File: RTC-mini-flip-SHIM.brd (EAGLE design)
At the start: 17.8 x 20.3 mm, 11 parts, among them IC1 DS3231/SO

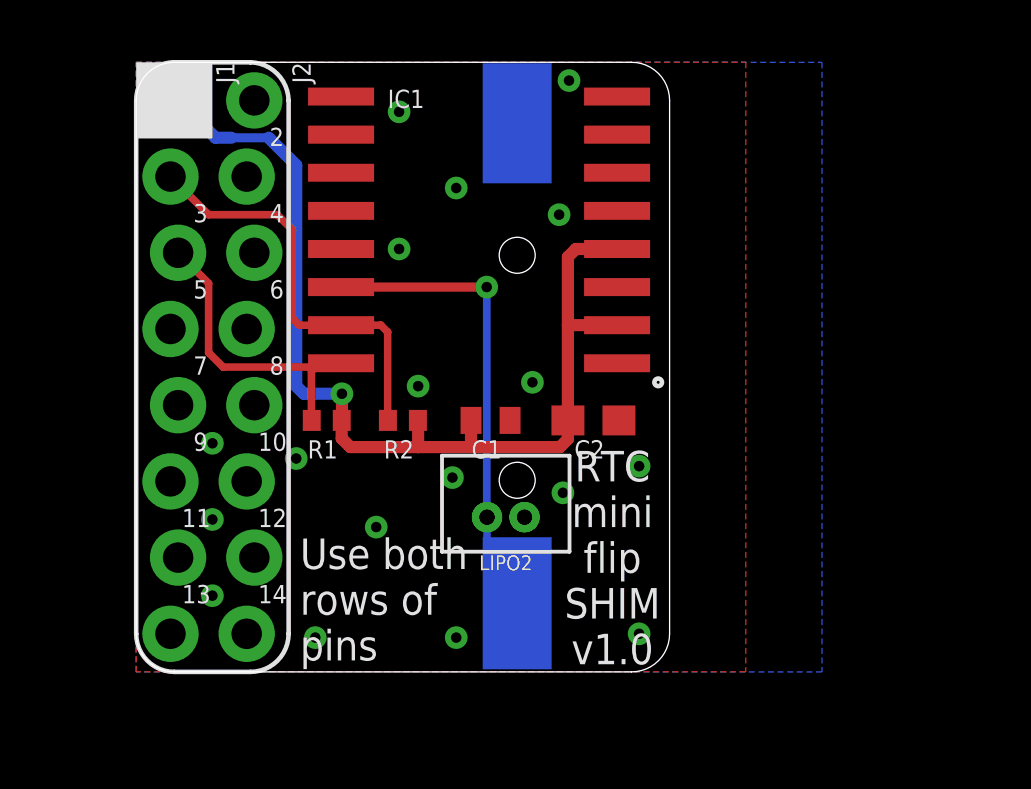
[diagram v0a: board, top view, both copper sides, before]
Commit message: Moved some stuff around. Add second footprint. Moved battery away from center for better flipability.
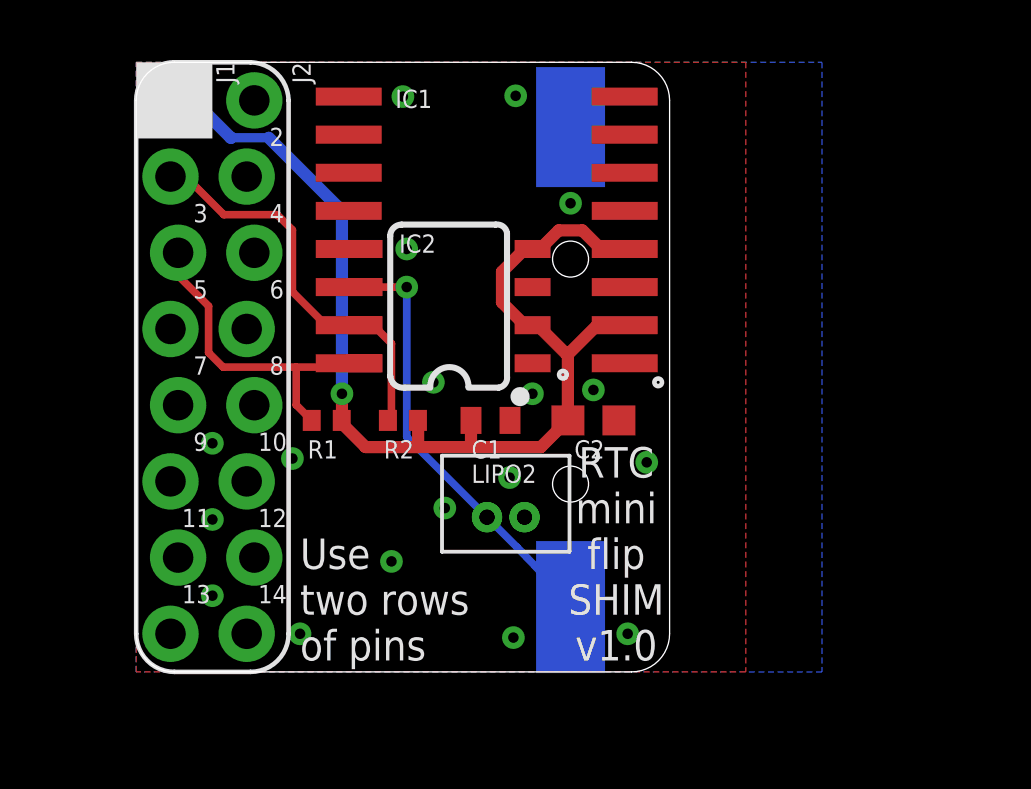
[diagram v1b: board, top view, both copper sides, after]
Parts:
- added IC2: DS3231M, SparkFun-Clocks:SO08
- moved LOGO1 1.91 mm to (23.2, 3.56)
- moved BAT1 1.78 mm to (14.5, 10.2)
- moved IC1 0.25 mm to (11.7, 14.7)
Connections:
- net 3.3V: now also IC2.2, IC2.4
- net GND: now also IC2.5
- net SCL: now also IC2.8
- net SDA: now also IC2.7
- net VBAT: now also IC2.6
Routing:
- net 3.3V: track 34.4 -> 37.5 mm
- net VBAT: track 15.8 -> 14.8 mm
- net SDA: track 14.1 -> 13.5 mm
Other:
- board text added: "Use two rows of pins"
- board text removed: "Use both rows of pins"

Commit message: Changed mini SHIM layout. Traced mini SHIM.
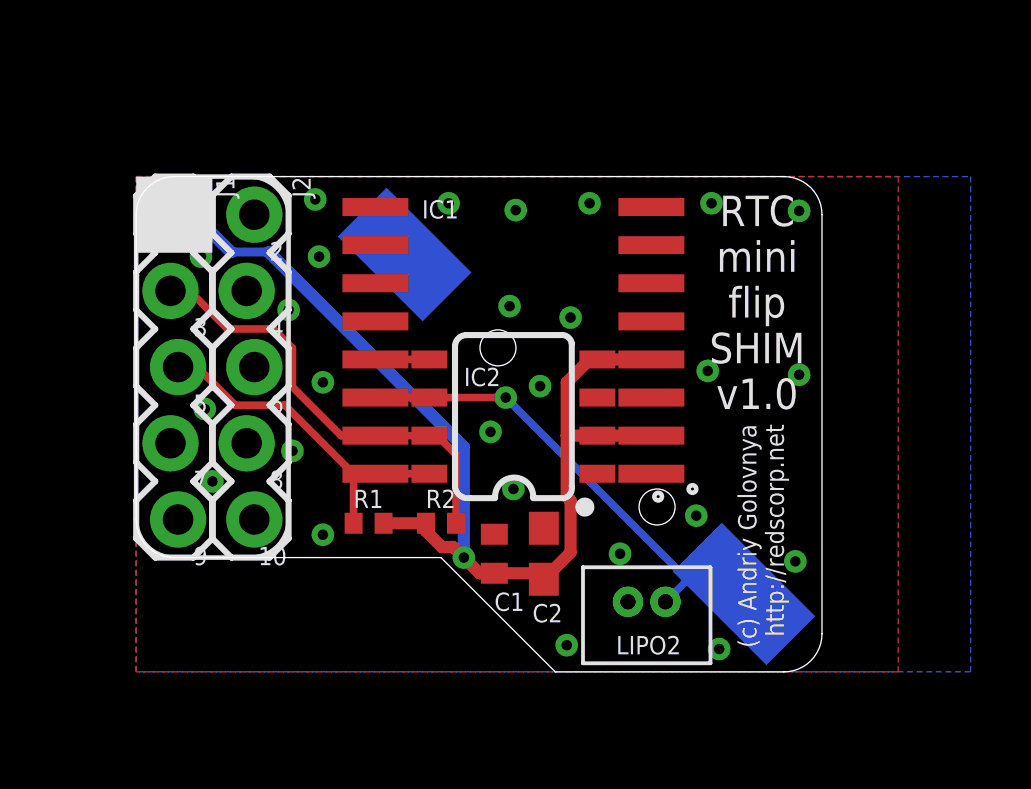
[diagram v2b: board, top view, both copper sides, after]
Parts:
- J1, J2: device SparkFun-Connectors:1X08_LOCK_NO_SILK -> SparkFun-Connectors:1X05_LOCK
- moved LIPO1 5.48 mm to (17.0, 2.34), turned to 0 degrees
- moved LIPO2 5.48 mm to (17.0, 2.34), turned to 180 degrees
- moved C2 4.74 mm to (13.6, 3.94), turned to 90 degrees
- moved C1 4.45 mm to (11.9, 3.94), turned to 90 degrees
- moved IC2 4.27 mm to (12.6, 8.51)
- moved J1 3.81 mm to (1.27, 15.2)
- moved J2 3.81 mm to (3.81, 15.2)
- moved IC1 3.79 mm to (12.6, 11.0)
- moved R1 3.70 mm to (7.75, 4.95)
- moved R2 3.66 mm to (10.2, 4.95), turned to 180 degrees
- moved BAT1 1.91 mm to (14.6, 8.26), turned to 315 degrees
- moved LOGO1 1.66 mm to (23.1, 1.91)
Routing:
- net 3.3V: track 37.5 -> 35.6 mm
- net GND: track 0.00 -> 1.80 mm, vias 18 -> 26
- net SDA: track 13.5 -> 14.8 mm
- net VBAT: track 14.8 -> 16.1 mm
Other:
- board size 17.8 x 20.3 mm -> 22.9 x 16.5 mm
- board text added: "+"
- board text added: "-"
- board text removed: "11"
- board text removed: "12"
- board text removed: "13"
- board text removed: "14"
- board text removed: "Use one rows of pins"
- board text removed: "Use two rows of pins"

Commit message: Use more locking pin headers. Moved some traces.
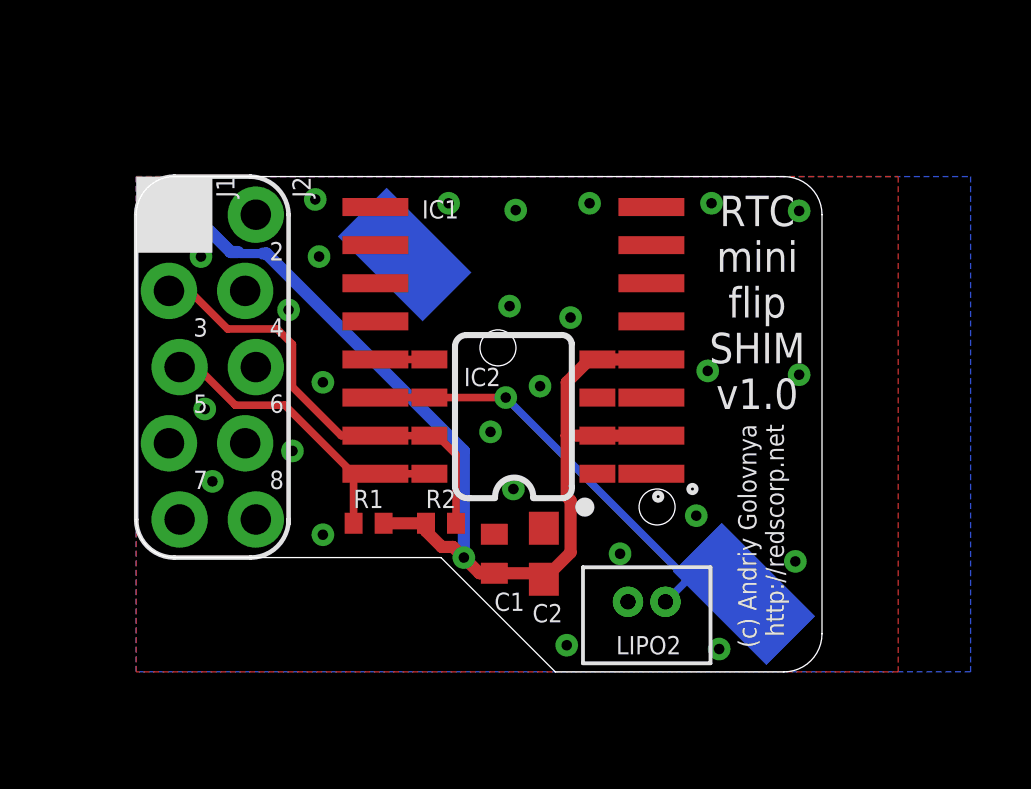
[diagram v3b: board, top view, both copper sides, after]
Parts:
- J1, J2: device SparkFun-Connectors:1X05_LOCK -> _my_locked_connectors:1X05_LOCK
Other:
- board text removed: "10"
- board text removed: "9"
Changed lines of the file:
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@@
 <layer number="115" name="ReferenceISLANDS" color="7" fill="1" visible="no" active="yes"/>
 <layer number="116" name="Patch_BOT" color="9" fill="4" visible="no" active="yes"/>
+<layer number="117" name="PM_Ref" color="7" fill="1" visible="no" active="no"/>
 <layer number="118" name="Rect_Pads" color="7" fill="1" visible="no" active="no"/>
+<layer number="119" name="PF_Ref" color="7" fill="1" visible="no" active="no"/>
+<layer number="120" name="WFL_Ref" color="7" fill="1" visible="no" active="no"/>
 <layer number="121" name="_tsilk" color="7" fill="1" visible="no" active="yes"/>
 <layer number="122" name="_bsilk" color="7" fill="1" visible="no" active="yes"/>
@@
 <layer number="128" name="_bValues" color="7" fill="1" visible="no" active="yes"/>
 <layer number="129" name="Mask" color="7" fill="1" visible="yes" active="yes"/>
+<layer number="130" name="SMDSTROOK" color="7" fill="1" visible="no" active="no"/>
 <layer number="131" name="tAdjust" color="7" fill="1" visible="no" active="yes"/>
 <layer number="132" name="bAdjust" color="7" fill="1" visible="no" active="yes"/>
+<layer number="133" name="bottom_silk" color="7" fill="1" visible="no" active="no"/>
+<layer number="134" name="silk_top" color="7" fill="1" visible="no" active="no"/>
+<layer number="135" name="silk_bottom" color="7" fill="1" visible="no" active="no"/>
+<layer number="136" name="silktop" color="7" fill="1" visible="no" active="no"/>
+<layer number="137" name="silkbottom" color="7" fill="1" visible="no" active="no"/>
+<layer number="138" name="EEE" color="7" fill="1" visible="no" active="no"/>
+<layer number="139" name="_tKeepout" color="7" fill="1" visible="no" active="no"/>
+<layer number="140" name="mbKeepout" color="7" fill="1" visible="no" active="no"/>
+<layer number="141" name="ASSEMBLY_TOP" color="7" fill="1" visible="no" active="no"/>
+<layer number="142" name="mbRestrict" color="7" fill="1" visible="no" active="no"/>
+<layer number="143" name="PLACE_BOUND_TOP" color="7" fill="1" visible="no" active="no"/>
 <layer number="144" name="Drill_legend" color="7" fill="1" visible="no" active="yes"/>
+<layer number="145" name="DrillLegend_01-16" color="7" fill="1" visible="no" active="no"/>
+<layer number="146" name="DrillLegend_01-20" color="7" fill="1" visible="no" active="no"/>
+<layer number="147" name="PIN_NUMBER" color="7" fill="1" visible="no" active="no"/>
+<layer number="148" name="DrillLegend_01-20" color="7" fill="1" visible="no" active="no"/>
+<layer number="149" name="DrillLegend_02-15" color="7" fill="1" visible="no" active="no"/>
 <layer number="150" name="Notes" color="7" fill="1" visible="no" active="yes"/>
 <layer number="151" name="HeatSink" color="7" fill="1" visible="no" active="yes"/>
@@
 <layer number="164" name="tRubout" color="7" fill="1" visible="yes" active="yes"/>
 <layer number="165" name="bRubout" color="7" fill="1" visible="yes" active="yes"/>
+<layer number="166" name="AntennaArea" color="7" fill="1" visible="no" active="no"/>
 <layer number="167" name="Fiducials" color="7" fill="1" visible="yes" active="yes"/>
+<layer number="168" name="4mmHeightArea" color="7" fill="1" visible="no" active="no"/>
 <layer number="169" name="internal" color="7" fill="1" visible="yes" active="yes"/>
+<layer number="191" name="mNets" color="7" fill="1" visible="no" active="no"/>
+<layer number="192" name="mBusses" color="7" fill="1" visible="no" active="no"/>
+<layer number="193" name="mPins" color="7" fill="1" visible="no" active="no"/>
+<layer number="194" name="mSymbols" color="7" fill="1" visible="no" active="no"/>
+<layer number="195" name="mNames" color="7" fill="1" visible="no" active="no"/>
+<layer number="196" name="mValues" color="7" fill="1" visible="no" active="no"/>
 <layer number="199" name="Contour" color="7" fill="1" visible="no" active="yes"/>
 <layer number="200" name="200bmp" color="1" fill="10" visible="no" active="yes"/>
@@
 <text x="1.905" y="6.096" size="0.6096" layer="21" font="vector" ratio="12">7</text>
 <text x="4.445" y="6.096" size="0.6096" layer="21" font="vector" ratio="12">8</text>
-<text x="1.905" y="3.556" size="0.6096" layer="21" font="vector" ratio="12">9</text>
-<text x="4.064" y="3.556" size="0.6096" layer="21" font="vector" ratio="12">10</text>
 <text x="0.635" y="11.176" size="0.6096" layer="22" font="vector" ratio="12" rot="MR0">3</text>
 <text x="0.635" y="8.636" size="0.6096" layer="22" font="vector" ratio="12" rot="MR0">5</text>
 <text x="0.635" y="6.096" size="0.6096" layer="22" font="vector" ratio="12" rot="MR0">7</text>
-<text x="0.635" y="3.556" size="0.6096" layer="22" font="vector" ratio="12" rot="MR0">9</text>
 <circle x="18.542" y="6.096" radius="0.127" width="0.1524" layer="21"/>
 <wire x1="5.08" y1="5.08" x2="3.81" y2="3.81" width="0.1524" layer="21" curve="-90"/>
@@
 <attribute name="VALUE" x="9.525" y="14.097" size="0.6096" layer="27" font="vector"/>
 </element>
-<element name="J1" library="SparkFun-Connectors" library_urn="urn:adsk.eagle:library:513" package="1X05_LOCK" package3d_urn="urn:adsk.eagle:package:38105/1" value="" x="1.27" y="15.24" smashed="yes" rot="R270">
+<element name="J1" library="_my_locked_connectors" package="1X05_LOCK" value="" x="1.27" y="15.24" smashed="yes" rot="R270">
 <attribute name="NAME" x="2.667" y="16.51" size="0.6096" layer="25" font="vector" rot="R270"/>
 <attribute name="VALUE" x="-0.762" y="16.51" size="0.6096" layer="27" font="vector" ratio="20" rot="R270"/>
 </element>
-<element name="J2" library="SparkFun-Connectors" library_urn="urn:adsk.eagle:library:513" package="1X05_LOCK" package3d_urn="urn:adsk.eagle:package:38105/1" value="" x="3.81" y="15.24" smashed="yes" rot="R270">
+<element name="J2" library="_my_locked_connectors" package="1X05_LOCK" value="" x="3.81" y="15.24" smashed="yes" rot="R270">
 <attribute name="NAME" x="5.207" y="16.51" size="0.6096" layer="25" font="vector" rot="R270"/>
 <attribute name="VALUE" x="1.778" y="16.51" size="0.6096" layer="27" font="vector" ratio="20" rot="R270"/>
@@
 <contactref element="J1" pad="3"/>
 <wire x1="3.302" y1="8.89" x2="2.032" y2="10.16" width="0.254" layer="1"/>
-<wire x1="1.397" y1="10.16" x2="2.032" y2="10.16" width="0.254" layer="1"/>
+<wire x1="1.4478" y1="10.16" x2="2.032" y2="10.16" width="0.254" layer="1"/>
 <wire x1="4.953" y1="8.89" x2="3.302" y2="8.89" width="0.254" layer="1"/>
 <wire x1="7.239" y1="6.604" x2="4.953" y2="8.89" width="0.254" layer="1"/>
@@
 <contactref element="R2" pad="1"/>
 <contactref element="J1" pad="2"/>
-<wire x1="1.143" y1="12.7" x2="1.778" y2="12.7" width="0.254" layer="1"/>
+<wire x1="1.0922" y1="12.7" x2="1.778" y2="12.7" width="0.254" layer="1"/>
 <wire x1="3.048" y1="11.43" x2="1.778" y2="12.7" width="0.254" layer="1"/>
-<wire x1="3.048" y1="11.43" x2="4.572" y2="11.43" width="0.254" layer="1"/>
-<wire x1="4.572" y1="11.43" x2="5.207" y2="10.795" width="0.254" layer="1"/>
-<wire x1="5.207" y1="9.4996" x2="5.207" y2="10.795" width="0.254" layer="1"/>
+<wire x1="3.048" y1="11.43" x2="4.699" y2="11.43" width="0.254" layer="1"/>
+<wire x1="4.699" y1="11.43" x2="5.207" y2="10.922" width="0.254" layer="1"/>
+<wire x1="5.207" y1="9.4996" x2="5.207" y2="10.922" width="0.254" layer="1"/>
 <contactref element="IC2" pad="7"/>
 <wire x1="7.973" y1="7.874" x2="6.8326" y2="7.874" width="0.254" layer="1"/>
@@
 <contactref element="R2" pad="2"/>
 <contactref element="J1" pad="1"/>
-<wire x1="1.397" y1="15.24" x2="1.905" y2="15.24" width="0.4064" layer="16"/>
-<wire x1="3.1496" y1="13.9954" x2="1.905" y2="15.24" width="0.4064" layer="16"/>
-<wire x1="3.1496" y1="13.9954" x2="3.175" y2="13.9954" width="0.4064" layer="16"/>
-<wire x1="3.175" y1="13.9954" x2="4.4196" y2="13.9954" width="0.3048" layer="16"/>
-<wire x1="4.4196" y1="13.9954" x2="10.922" y2="7.493" width="0.4064" layer="16"/>
-<wire x1="10.922" y1="7.493" x2="10.922" y2="3.81" width="0.4064" layer="16"/>
+<wire x1="10.922" y1="3.81" x2="10.922" y2="7.366" width="0.4064" layer="16"/>
 <via x="10.922" y="3.81" extent="1-16" drill="0.35"/>
 <contactref element="IC2" pad="4"/>
@@
 <wire x1="15.373" y1="7.874" x2="14.351" y2="7.874" width="0.4064" layer="1"/>
 <wire x1="15.373" y1="7.874" x2="17.173" y2="7.874" width="0.4064" layer="1"/>
+<wire x1="1.4478" y1="15.24" x2="1.905" y2="15.24" width="0.4064" layer="16"/>
+<wire x1="3.400425" y1="13.9954" x2="3.1496" y2="13.9954" width="0.4064" layer="16"/>
+<wire x1="3.1496" y1="13.9954" x2="1.905" y2="15.24" width="0.4064" layer="16"/>
+<wire x1="4.3434" y1="13.9446" x2="4.219575" y2="13.9446" width="0.4064" layer="16"/>
+<wire x1="10.922" y1="7.366" x2="4.3434" y2="13.9446" width="0.4064" layer="16"/>
+<wire x1="4.219575" y1="13.9446" x2="3.451225" y2="13.9446" width="0.3048" layer="16"/>
+<wire x1="3.451225" y1="13.9446" x2="3.400425" y2="13.9954" width="0.3048" layer="16"/>
 </signal>
 <signal name="GND" airwireshidden="yes">

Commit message: Moved battery socket to another side to not collide with CPU heat sink. Generated CAM files.
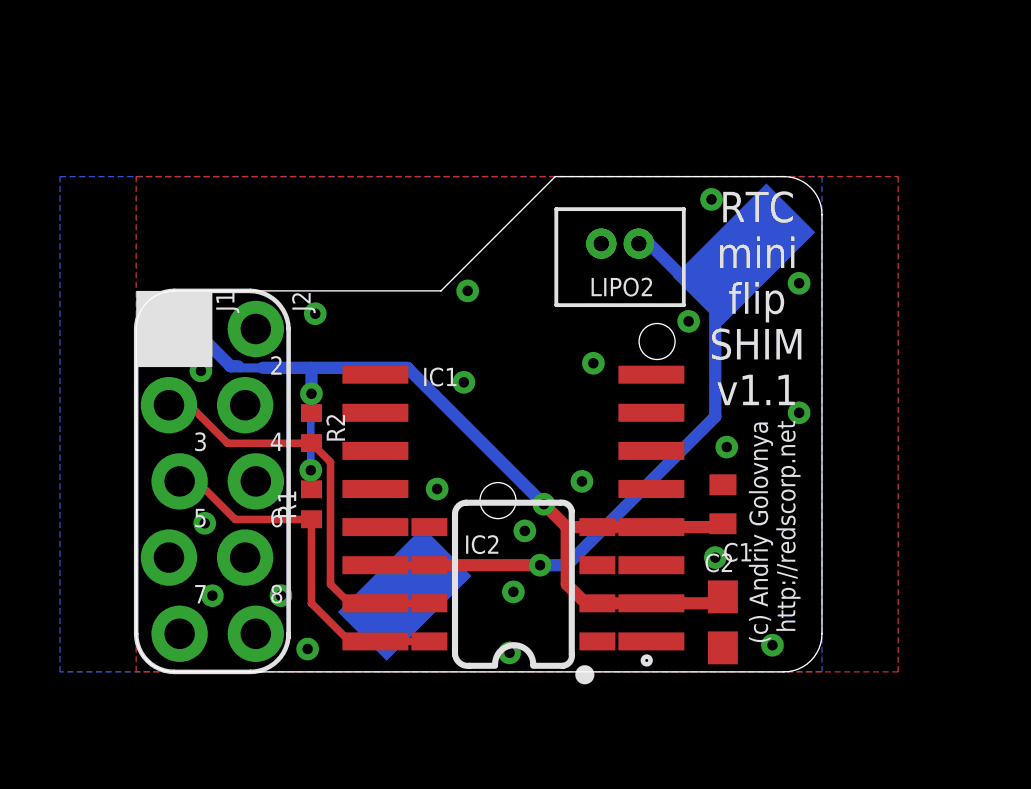
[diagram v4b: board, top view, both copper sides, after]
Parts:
- moved LIPO1 12.0 mm to (16.1, 14.3)
- moved LIPO2 12.0 mm to (16.1, 14.3)
- moved C1 7.80 mm to (19.6, 5.59)
- moved C2 6.39 mm to (19.6, 1.65), turned to 270 degrees
- moved IC2 5.59 mm to (12.6, 2.92)
- moved IC1 5.59 mm to (12.6, 5.46)
- moved R2 5.36 mm to (5.84, 8.13), turned to 90 degrees
- moved J1 3.81 mm to (1.27, 11.4)
- moved J2 3.81 mm to (3.81, 11.4)
- moved R1 2.01 mm to (5.84, 5.59), turned to 90 degrees
- moved LOGO1 0.28 mm to (23.0, 1.65)
- turned BAT1 to 225 degrees
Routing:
- net VBAT: track 16.1 -> 23.4 mm
- net 3.3V: track 35.5 -> 33.1 mm, vias 1 -> 3
- net GND: track 1.80 -> 0.00 mm, vias 26 -> 21
- net SDA: track 15.0 -> 13.8 mm
- net SCL: track 11.5 -> 12.2 mm
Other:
- outline, holes or cut-outs redrawn
- board text added: "RTC mini flip SHIM v1.1"
- board text removed: "RTC mini flip SHIM v1.0"
